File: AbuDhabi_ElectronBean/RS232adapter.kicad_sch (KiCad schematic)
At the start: 7 parts, among them SW1 SW_DPST, U3 MAX3232

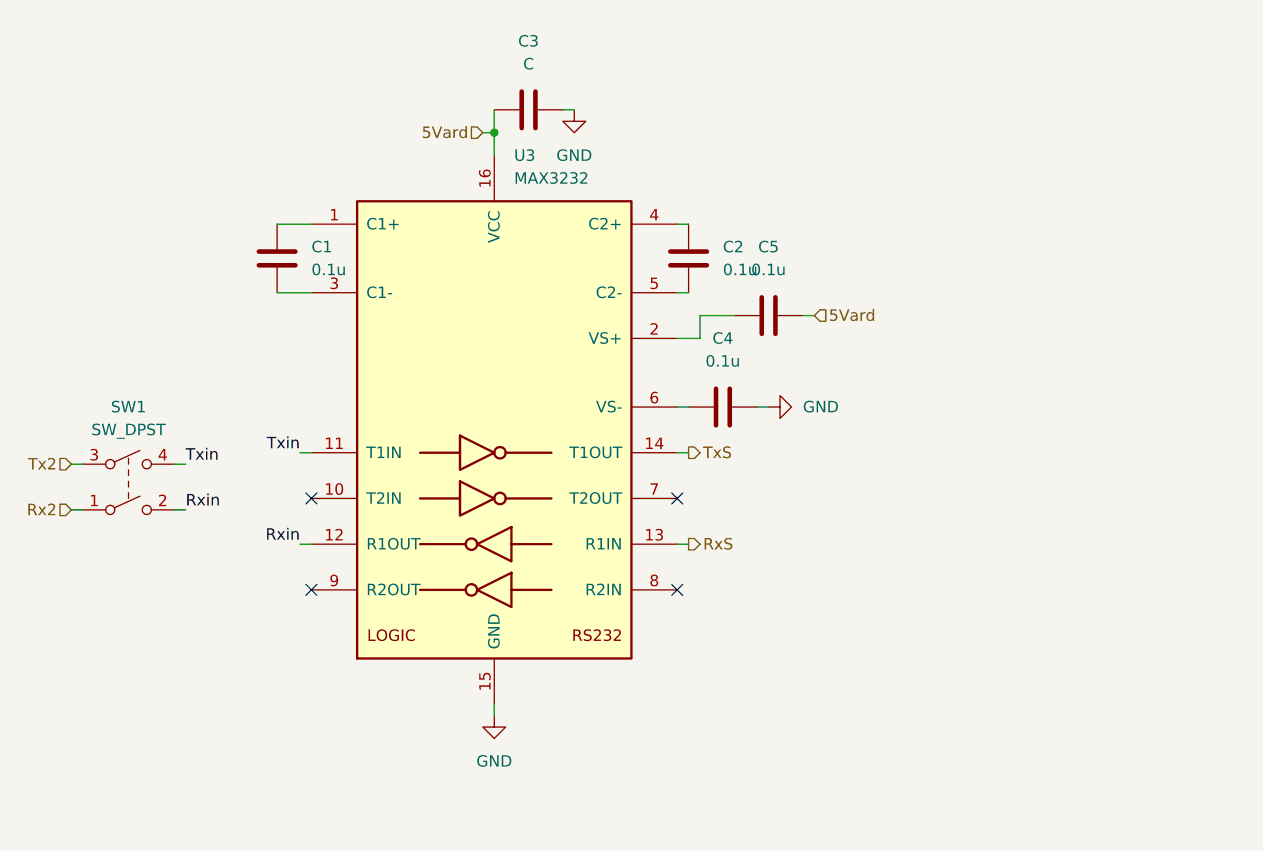
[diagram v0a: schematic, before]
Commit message: RS232 interface changes (completed) and RS485 interface in working...
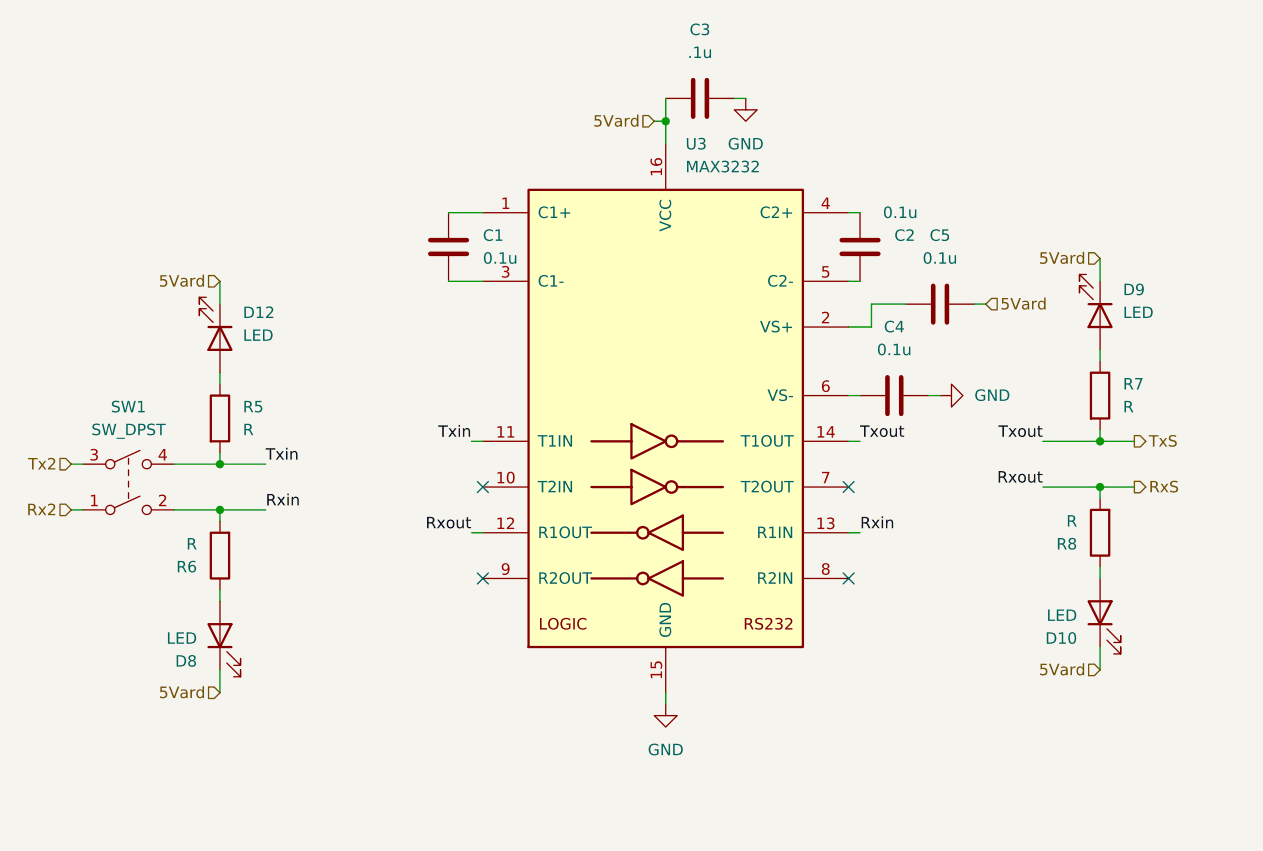
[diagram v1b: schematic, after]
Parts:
- added D10, D12, D8, D9: LED, symbol Device:LED
- added R5, R6, R7, R8: R, symbol Device:R
- C3: value C -> .1u
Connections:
- net 5Vard: now also D10.1 (K), D12.1 (K), D8.1 (K), D9.1 (K)
- net RxS: now also U3.12 (R1OUT), R8.2; no longer U3.13 (R1IN)
- net Rxin: now also U3.13 (R1IN), R6.2; no longer U3.12 (R1OUT)
- net TxS: now also R7.2
- net Txin: now also R5.2
- new net: D9.2 (A), R7.1
- new net: D8.2 (A), R6.1
- new net: D12.2 (A), R5.1
- new net: D10.2 (A), R8.1
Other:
- moved on the sheet: C1, C2, C3, C4, C5, U3

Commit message: Main board file updated. Added Arduino code for the LCD
The LCD is not working yet though.
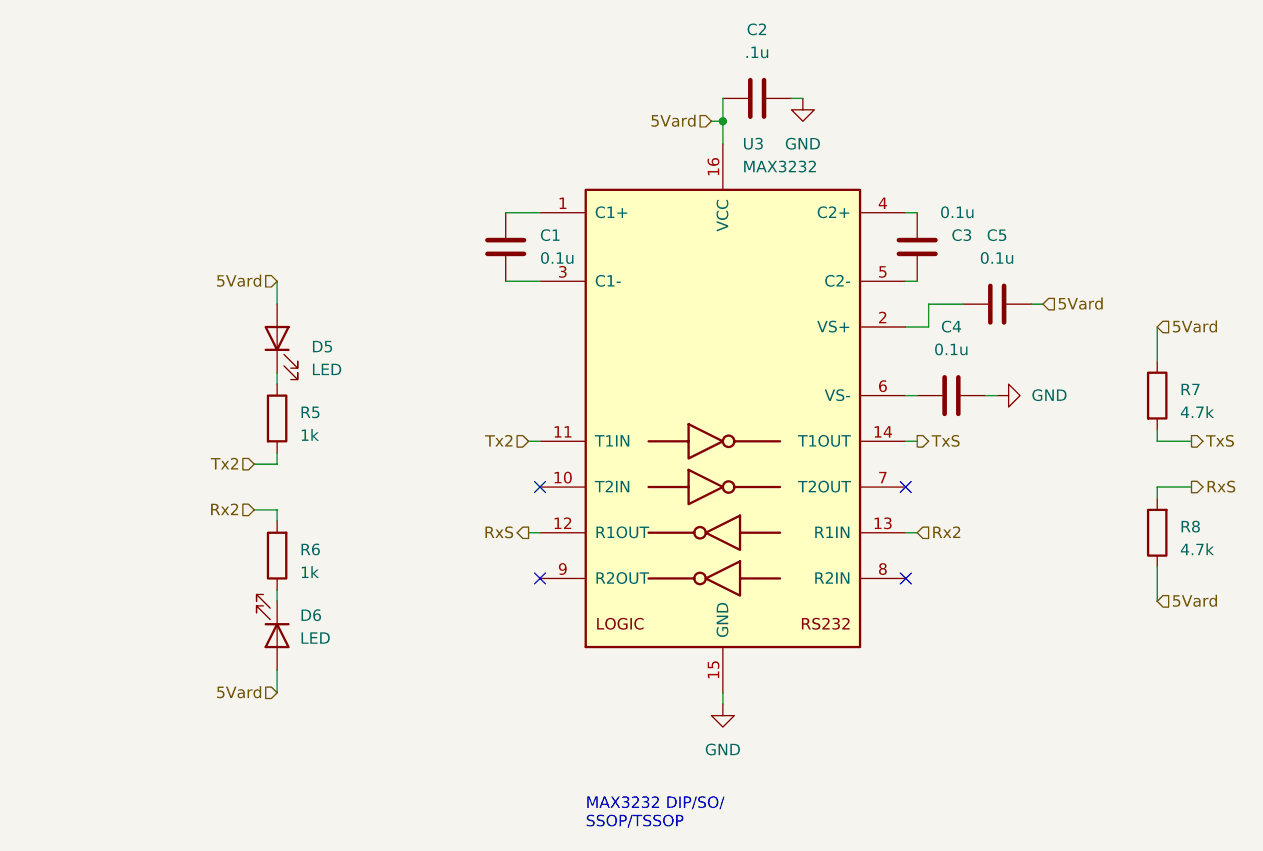
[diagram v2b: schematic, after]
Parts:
- removed D10, D12, D8, D9: LED, symbol Device:LED
- removed SW1: SW_DPST, symbol Switch:SW_DPST
- added D5: LED, LED_SMD:LED_0603_1608Metric, symbol Device:LED
- added D6: LED, LED_SMD:LED_0603_1608Metric_Pad1.05x0.95mm_HandSolder, symbol Device:LED
- C1, C4, C5: footprint (none) -> Capacitor_SMD:C_0603_1608Metric
- C2: value 0.1u -> .1u; footprint (none) -> Capacitor_SMD:C_0603_1608Metric
- C3: value .1u -> 0.1u; footprint (none) -> Capacitor_SMD:C_0603_1608Metric
- R5, R6: value R -> 1k; footprint (none) -> Resistor_SMD:R_0603_1608Metric
- R7, R8: value R -> 4.7k; footprint (none) -> Resistor_SMD:R_0603_1608Metric
- U3: footprint (none) -> Package_SO:SOIC-16_3.9x9.9mm_P1.27mm
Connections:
- net Rxin is gone; now on net Rx2: R6.2, U3.13 (R1IN)
- net Txin is gone; now on net Tx2: R5.2, U3.11 (T1IN)
- net 5Vard: now also C2.1, R7.1, R8.1, D5.2 (A), D6.2 (A); no longer C3.1
- net GND: now also C2.2; no longer C3.2
- net at U3.4 (C2+): now also C3.1; no longer C2.1
- net at U3.5 (C2-): now also C3.2; no longer C2.2
- net at R6.1: now also D6.1 (K)
- net at R5.1: now also D5.1 (K)
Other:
- note added: "MAX3232 DIP/SO/ SSOP/TSSOP"
